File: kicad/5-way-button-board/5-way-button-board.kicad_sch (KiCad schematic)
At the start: 12 parts, among them J1 Conn_01x06_Pin, J2 Conn_01x06_Pin, SW6 SW_Push_LEDx5

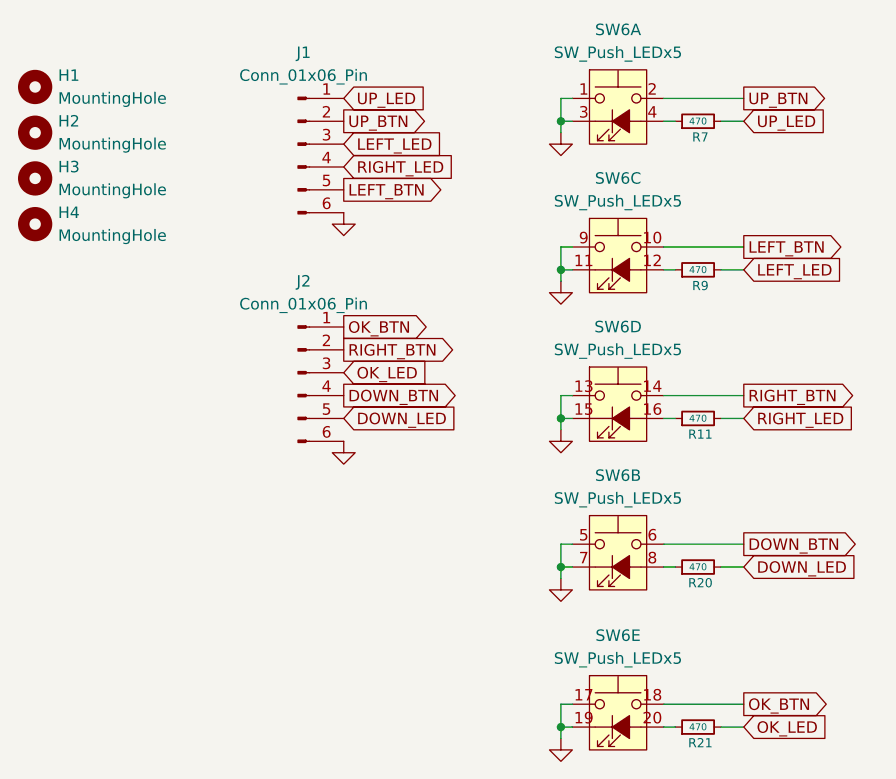
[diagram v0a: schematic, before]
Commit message: Add encoder board
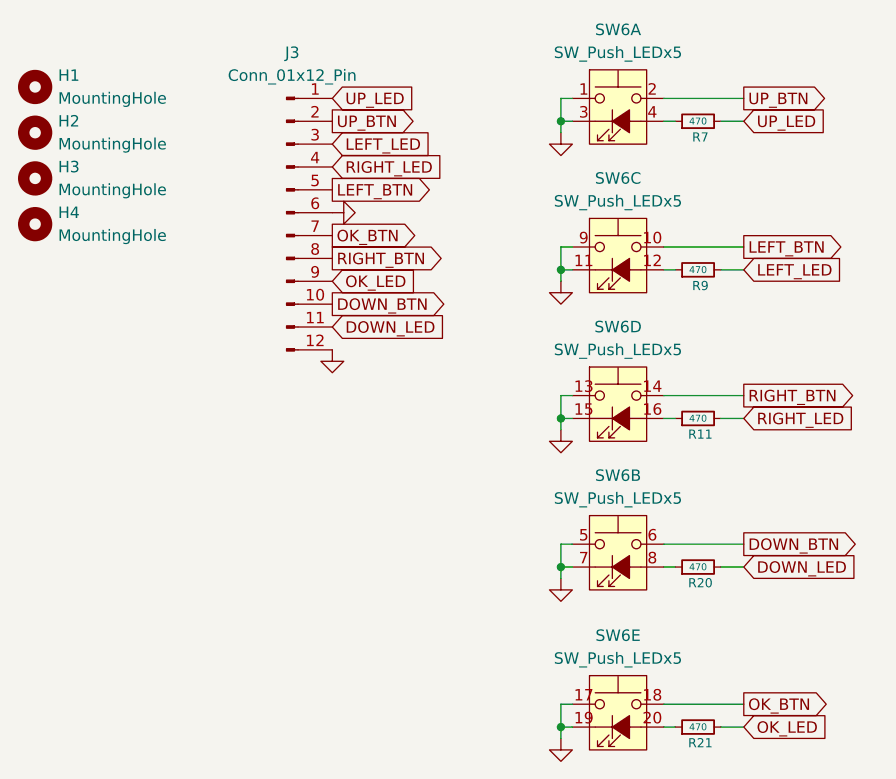
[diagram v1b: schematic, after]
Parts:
- removed J1, J2: Conn_01x06_Pin, Connector_PinHeader_2.00mm:PinHeader_1x06_P2.00mm_Vertical, symbol Connector:Conn_01x06_Pin
- added J3: Conn_01x12_Pin, Connector_PinHeader_2.54mm:PinHeader_1x12_P2.54mm_Vertical, symbol Connector:Conn_01x12_Pin
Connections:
- net DOWN_BTN: now also J3.10 (Pin_10)
- net DOWN_LED: now also J3.11 (Pin_11)
- net GND: now also J3.12 (Pin_12), J3.6 (Pin_6)
- net LEFT_BTN: now also J3.5 (Pin_5)
- net LEFT_LED: now also J3.3 (Pin_3)
- net OK_BTN: now also J3.7 (Pin_7)
- net OK_LED: now also J3.9 (Pin_9)
- net RIGHT_BTN: now also J3.8 (Pin_8)
- net RIGHT_LED: now also J3.4 (Pin_4)
- net UP_BTN: now also J3.2 (Pin_2)
- net UP_LED: now also J3.1 (Pin_1)
